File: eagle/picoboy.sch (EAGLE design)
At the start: 9 parts

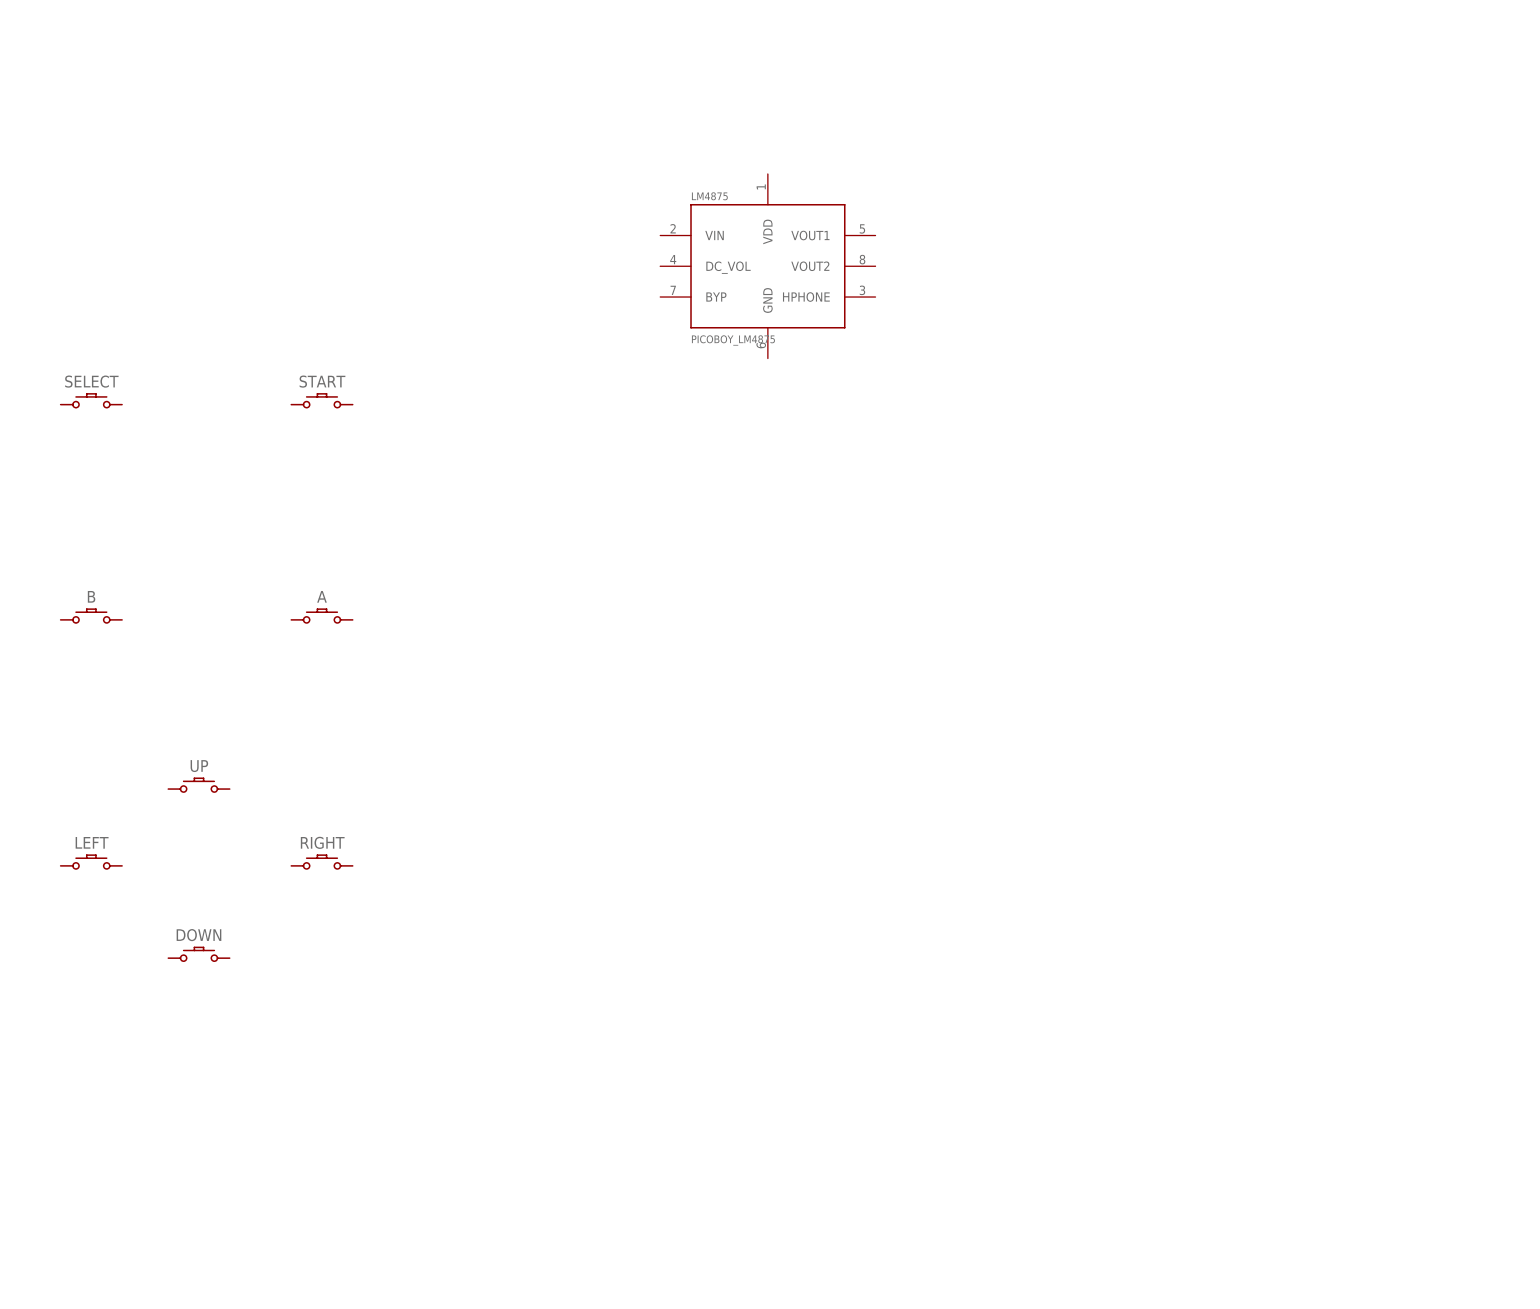
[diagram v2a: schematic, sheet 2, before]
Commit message: Start amplifier schematics
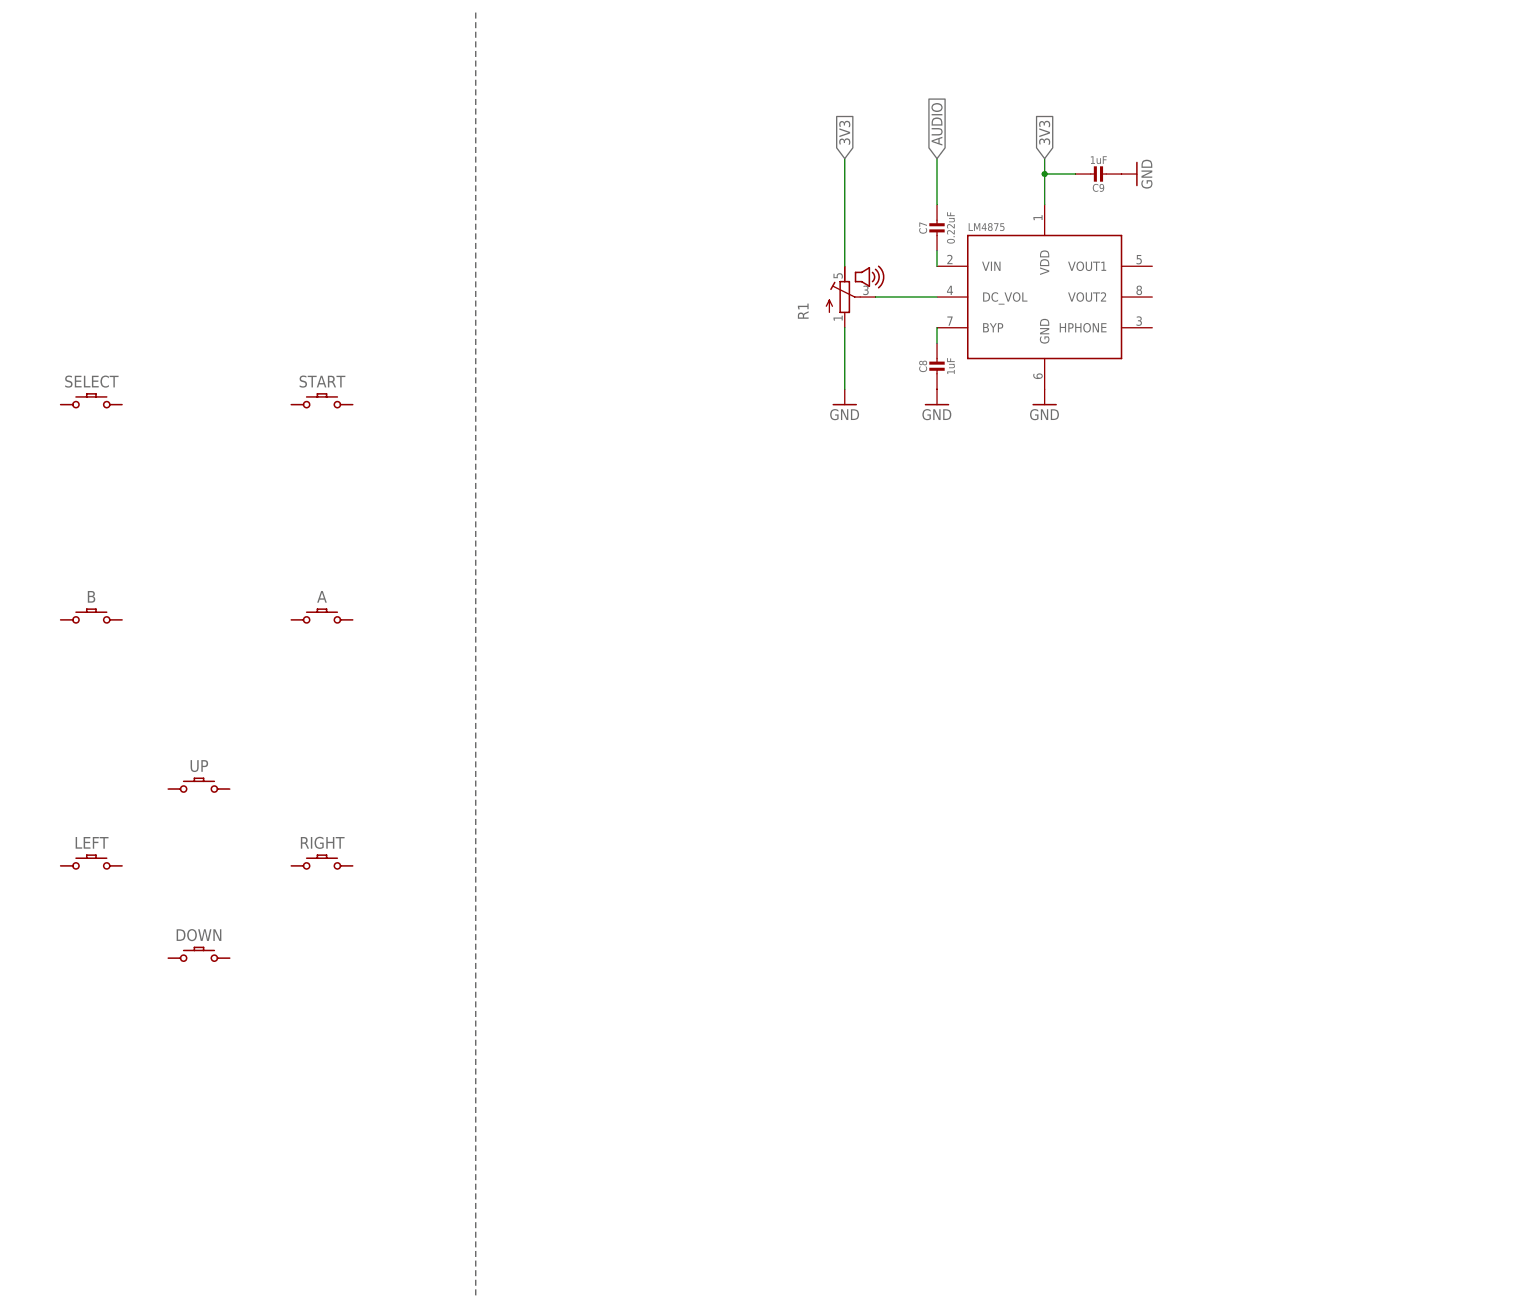
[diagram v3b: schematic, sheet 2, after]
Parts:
- added C7: 0.22uF, picoboy:PICOBOY_CAPACITOR_CERAMIC
- added C8, C9: 1uF, picoboy:PICOBOY_CAPACITOR_CERAMIC
- added R1: (no value), picoboy:PICOBOY_VOLUME_WHEEL
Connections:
- new net 3V3: R1.E
- new net AUDIO: C7.1
- new net GND: C8.2, C9.2, LM4875.GND, R1.A
- new net N$1: C8.1, LM4875.BYP
- new net N$2: C9.1, LM4875.VDD
- new net N$3: C7.2, LM4875.VIN
- new net N$4: LM4875.DC_VOL, R1.S
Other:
- moved on the sheet: LM4875
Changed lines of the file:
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@@
 <layer number="93" name="Pins" color="2" fill="1" visible="no" active="yes"/>
 <layer number="94" name="Symbols" color="4" fill="1" visible="yes" active="yes"/>
-<layer number="95" name="Names" color="7" fill="1" visible="yes" active="yes"/>
+<layer number="95" name="Names" color="3" fill="1" visible="yes" active="yes"/>
 <layer number="96" name="Values" color="7" fill="1" visible="yes" active="yes"/>
-<layer number="97" name="Info" color="7" fill="1" visible="yes" active="yes"/>
+<layer number="97" name="Info" color="15" fill="1" visible="yes" active="yes"/>
 <layer number="98" name="Guide" color="6" fill="1" visible="yes" active="yes"/>
 <layer number="99" name="SpiceOrder" color="7" fill="1" visible="yes" active="yes"/>
@@
 <part name="START" library="picoboy" deviceset="PICOBOY_CONDUCTIVE_BUTTON_STARTSELECT" device="CONDUCTIVE_BUTTON_THICK_STARTSELECT"/>
 <part name="LM4875" library="picoboy" deviceset="PICOBOY_LM4875" device=""/>
+<part name="GND1" library="supply1" library_urn="urn:adsk.eagle:library:371" deviceset="GND" device=""/>
+<part name="GND2" library="supply1" library_urn="urn:adsk.eagle:library:371" deviceset="GND" device=""/>
+<part name="GND3" library="supply1" library_urn="urn:adsk.eagle:library:371" deviceset="GND" device=""/>
+<part name="C8" library="picoboy" deviceset="PICOBOY_CAPACITOR_CERAMIC" device="" value="1uF"/>
+<part name="C9" library="picoboy" deviceset="PICOBOY_CAPACITOR_CERAMIC" device="" value="1uF"/>
+<part name="C7" library="picoboy" deviceset="PICOBOY_CAPACITOR_CERAMIC" device="" value="0.22uF"/>
+<part name="R1" library="picoboy" deviceset="PICOBOY_VOLUME_WHEEL" device=""/>
+<part name="GND4" library="supply1" library_urn="urn:adsk.eagle:library:371" deviceset="GND" device=""/>
 </parts>
 <sheets>
@@
 <sheet>
 <plain>
+<wire x1="101.6" y1="212.09" x2="101.6" y2="0" width="0.1524" layer="97" style="shortdash"/>
 </plain>
 <instances>
@@
 <attribute name="NAME" x="76.2" y="151.13" size="1.9304" layer="95" font="vector" ratio="20" align="center"/>
 </instance>
-<instance part="LM4875" gate="U$1" x="142.24" y="170.18" smashed="yes">
-<attribute name="NAME" x="137.16" y="181.102" size="1.27" layer="95"/>
-<attribute name="VALUE" x="137.16" y="157.48" size="1.27" layer="96"/>
+<instance part="LM4875" gate="U$1" x="187.96" y="165.1" smashed="yes">
+<attribute name="NAME" x="182.88" y="176.022" size="1.27" layer="95"/>
+<attribute name="VALUE" x="182.88" y="152.4" size="1.27" layer="96" display="off"/>
+</instance>
+<instance part="GND1" gate="1" x="195.58" y="147.32" smashed="yes">
+<attribute name="VALUE" x="193.04" y="144.78" size="1.778" layer="96"/>
+</instance>
+<instance part="GND2" gate="1" x="210.82" y="185.42" smashed="yes" rot="R90">
+<attribute name="VALUE" x="213.36" y="182.88" size="1.778" layer="96" rot="R90"/>
+</instance>
+<instance part="GND3" gate="1" x="177.8" y="147.32" smashed="yes">
+<attribute name="VALUE" x="175.26" y="144.78" size="1.778" layer="96"/>
+</instance>
+<instance part="C8" gate="G$1" x="177.8" y="152.4" smashed="yes">
+<attribute name="NAME" x="175.51" y="153.65" size="1.27" layer="95" font="vector" rot="R90" align="center"/>
+<attribute name="VALUE" x="180.1" y="153.65" size="1.27" layer="96" font="vector" rot="R90" align="center"/>
+<attribute name="VALUE" x="180.1" y="153.65" size="1.27" layer="96" font="vector" rot="R90" align="center"/>
+</instance>
+<instance part="C9" gate="G$1" x="205.74" y="185.42" smashed="yes" rot="R90">
+<attribute name="NAME" x="204.49" y="183.13" size="1.27" layer="95" font="vector" rot="R180" align="center"/>
+<attribute name="VALUE" x="204.49" y="187.72" size="1.27" layer="96" font="vector" rot="R180" align="center"/>
+<attribute name="NAME" x="204.49" y="183.13" size="1.27" layer="95" font="vector" rot="R180" align="center"/>
+<attribute name="VALUE" x="204.49" y="187.72" size="1.27" layer="96" font="vector" rot="R180" align="center"/>
+</instance>
+<instance part="C7" gate="G$1" x="177.8" y="175.26" smashed="yes">
+<attribute name="NAME" x="175.51" y="176.51" size="1.27" layer="95" font="vector" rot="R90" align="center"/>
+<attribute name="VALUE" x="180.1" y="176.51" size="1.27" layer="96" font="vector" rot="R90" align="center"/>
+<attribute name="NAME" x="175.51" y="176.51" size="1.27" layer="95" font="vector" rot="R90" align="center"/>
+<attribute name="VALUE" x="180.1" y="176.51" size="1.27" layer="96" font="vector" rot="R90" align="center"/>
+</instance>
+<instance part="R1" gate="R$1" x="162.56" y="165.1" smashed="yes">
+<attribute name="NAME" x="156.591" y="161.29" size="1.778" layer="95" rot="R90"/>
+<attribute name="VALUE" x="158.75" y="161.29" size="1.778" layer="96" rot="R90"/>
+</instance>
+<instance part="GND4" gate="1" x="162.56" y="147.32" smashed="yes">
+<attribute name="VALUE" x="160.02" y="144.78" size="1.778" layer="96"/>
 </instance>
 </instances>
@@
 </busses>
 <nets>
+<net name="GND" class="0">
+<segment>
+<pinref part="LM4875" gate="U$1" pin="GND"/>
+<pinref part="GND1" gate="1" pin="GND"/>
+</segment>
+<segment>
+<pinref part="GND2" gate="1" pin="GND"/>
+<pinref part="C9" gate="G$1" pin="2"/>
+</segment>
+<segment>
+<pinref part="GND3" gate="1" pin="GND"/>
+<pinref part="C8" gate="G$1" pin="2"/>
+</segment>
+<segment>
+<pinref part="R1" gate="R$1" pin="A"/>
+<pinref part="GND4" gate="1" pin="GND"/>
+<wire x1="162.56" y1="160.02" x2="162.56" y2="149.86" width="0.1524" layer="91"/>
+</segment>
+</net>
+<net name="N$1" class="0">
+<segment>
+<pinref part="LM4875" gate="U$1" pin="BYP"/>
+<wire x1="177.8" y1="157.48" x2="177.8" y2="160.02" width="0.1524" layer="91"/>
+<pinref part="C8" gate="G$1" pin="1"/>
+</segment>
+</net>
+<net name="N$2" class="0">
+<segment>
+<pinref part="LM4875" gate="U$1" pin="VDD"/>
+<wire x1="195.58" y1="180.34" x2="195.58" y2="185.42" width="0.1524" layer="91"/>
+<wire x1="195.58" y1="185.42" x2="200.66" y2="185.42" width="0.1524" layer="91"/>
+<pinref part="C9" gate="G$1" pin="1"/>
+<wire x1="195.58" y1="187.96" x2="195.58" y2="185.42" width="0.1524" layer="91"/>
+<junction x="195.58" y="185.42"/>
+</segment>
+</net>
+<net name="N$3" class="0">
+<segment>
+<pinref part="LM4875" gate="U$1" pin="VIN"/>
+<pinref part="C7" gate="G$1" pin="2"/>
+<wire x1="177.8" y1="172.72" x2="177.8" y2="170.18" width="0.1524" layer="91"/>
+</segment>
+</net>
+<net name="N$4" class="0">
+<segment>
+<pinref part="R1" gate="R$1" pin="S"/>
+<pinref part="LM4875" gate="U$1" pin="DC_VOL"/>
+<wire x1="167.64" y1="165.1" x2="177.8" y2="165.1" width="0.1524" layer="91"/>
+</segment>
+</net>
+<net name="3V3" class="0">
+<segment>
+<pinref part="R1" gate="R$1" pin="E"/>
+<label x="162.56" y="187.96" size="1.778" layer="95" rot="R90" xref="yes"/>
+<wire x1="162.56" y1="187.96" x2="162.56" y2="170.18" width="0.1524" layer="91"/>
+<label x="195.58" y="187.96" size="1.778" layer="95" rot="R90" xref="yes"/>
+</segment>
+</net>
+<net name="AUDIO" class="0">
+<segment>
+<pinref part="C7" gate="G$1" pin="1"/>
+<wire x1="177.8" y1="180.34" x2="177.8" y2="187.96" width="0.1524" layer="91"/>
+<label x="177.8" y="187.96" size="1.778" layer="95" rot="R90" xref="yes"/>
+</segment>
+</net>
 </nets>
 </sheet>

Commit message: Wired all audio components
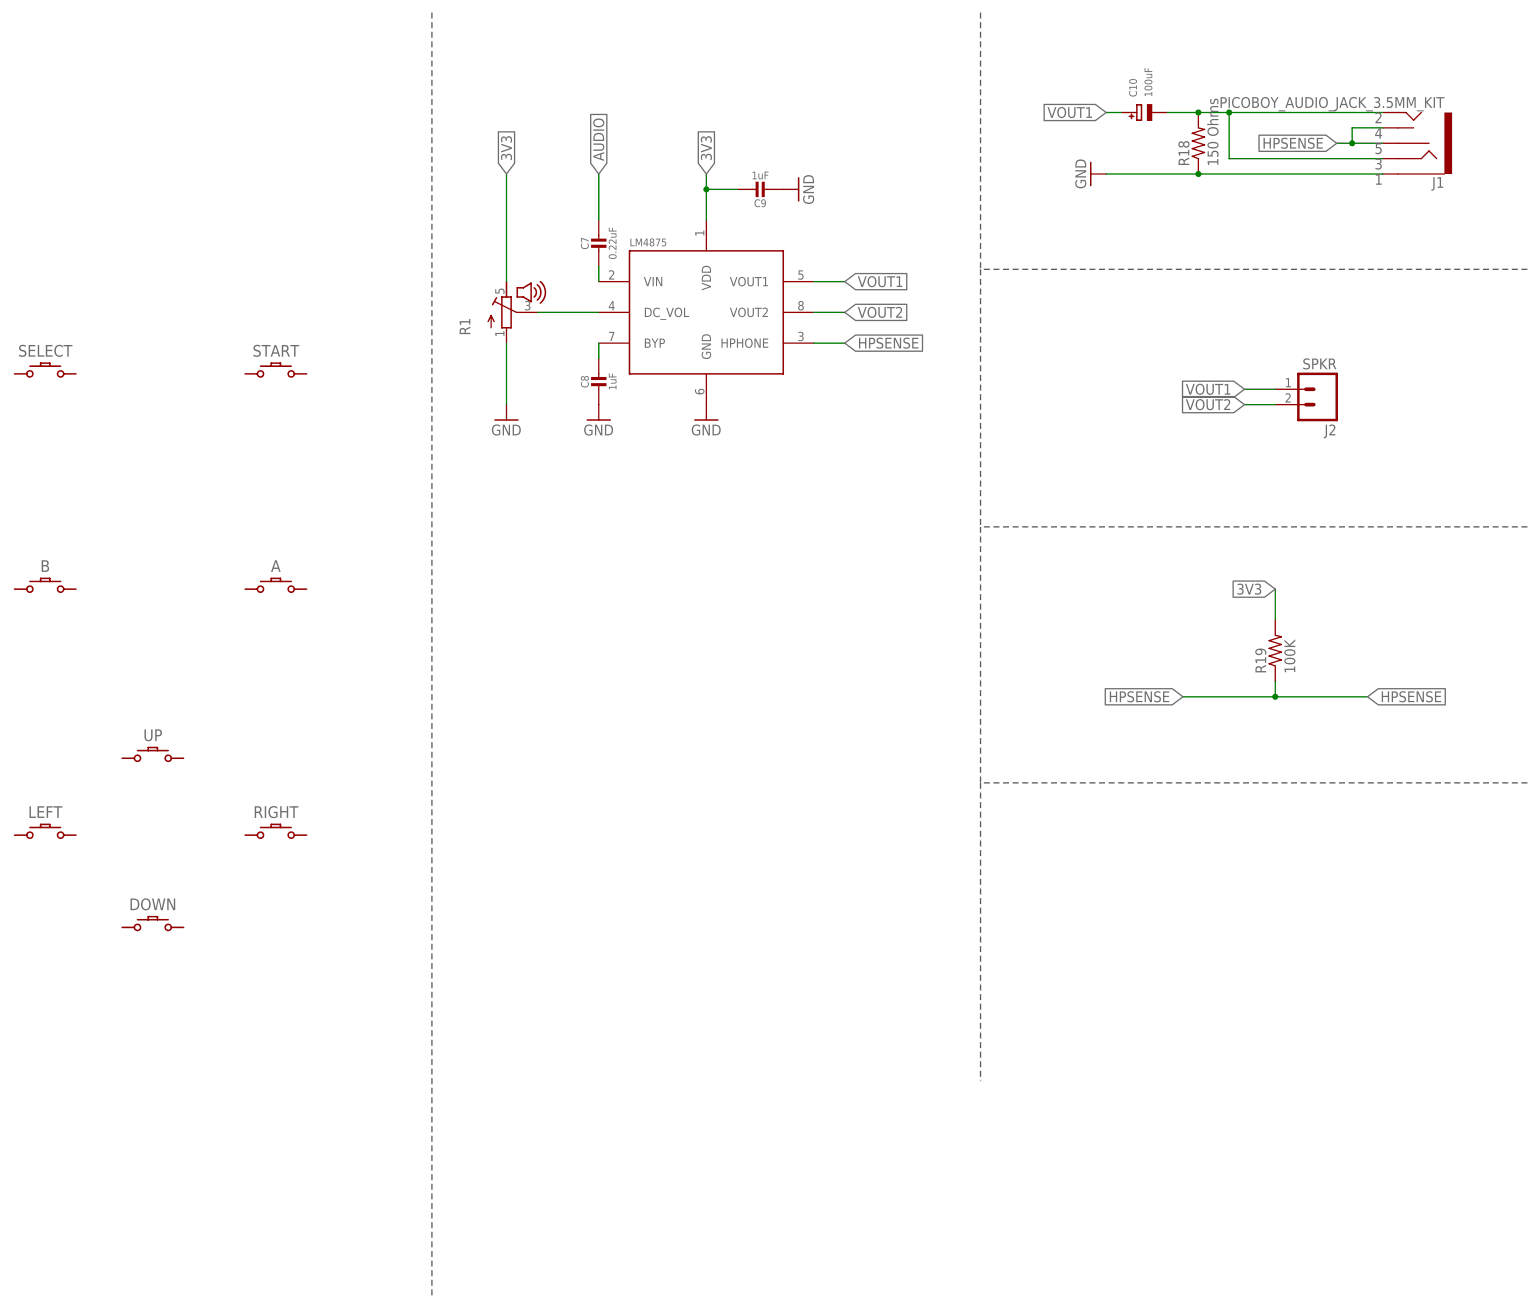
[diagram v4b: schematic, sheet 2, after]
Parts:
- added C10: 100uF, picoboy:PICOBOY_CAPACITOR_TANTALUMA/3216_WAVE
- added J1: PICOBOY_AUDIO_JACK_3.5MM_KIT, picoboy:PICOBOY_AUDIO_JACK_3.5MM_KIT
- added J2: SPKR, con-amp-quick:M02
- added R18: 150 Ohms, rcl:R-US_R0603
- added R19: 100K, rcl:R-US_R0603
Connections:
- net N$1 renamed BYP
- net N$3 renamed VIN
- net N$4 renamed DC_VOL
- removed net N$2: C9.1, LM4875.VDD
- new net HPSENSE: J1.RSH, J1.TSH, LM4875.HPHONE, R19.1
- new net N$7: C10.-, J1.RING, J1.TIP, R18.2
- new net VOUT1: C10.+, J2.1, LM4875.VOUT1
- new net VOUT2: J2.2, LM4875.VOUT2
- net 3V3: now also C9.1, LM4875.VDD, R19.2
- net GND: now also J1.SLEEVE, R18.1
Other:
- moved on the sheet: A, B, C7, C8, C9, DOWN, LEFT, LM4875, R1, RIGHT, SELECT, START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
